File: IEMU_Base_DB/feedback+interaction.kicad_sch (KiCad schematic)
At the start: 37 parts, among them J401 SJ3-35083C-TR, Q401 CSD13381F4, SW401 TS-1088-AR02016, U401 SN74LVC1T45DCKR, U402 DRV5032FADBZR

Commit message: swapped the coin cell vibration actuator pins
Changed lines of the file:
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@@
 	(text "Connector, Lid-Sensor, LEDs & Buttons"
 		(exclude_from_sim no)
-		(at 58.928 25.146 0)
+		(at 78.74 24.892 0)
 		(effects
 			(font

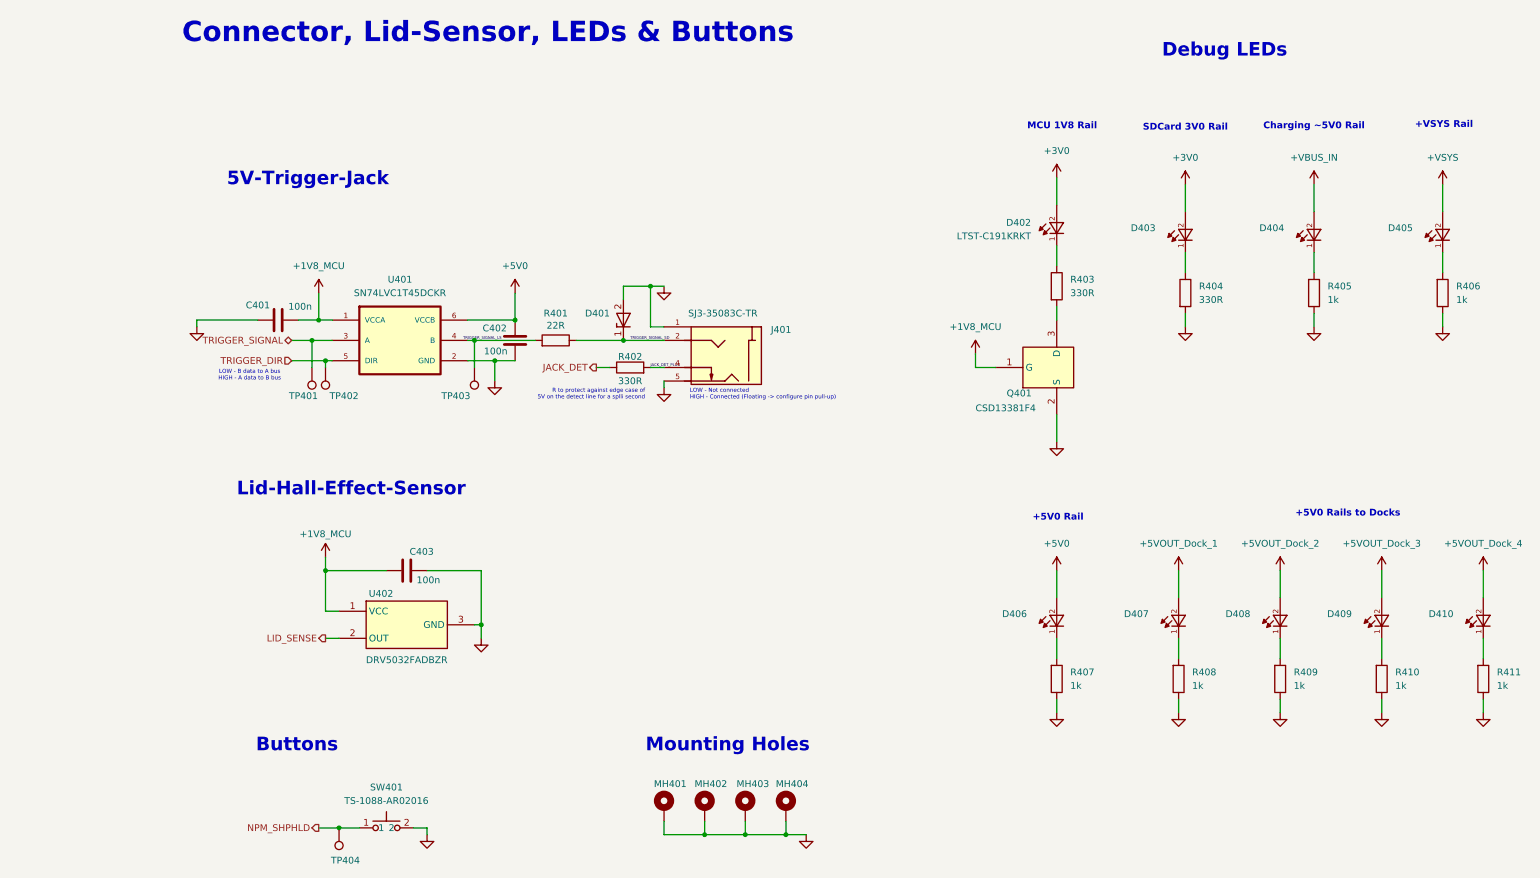
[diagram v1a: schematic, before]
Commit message: implemented changes from the review with TF and fixed lost parts in the library
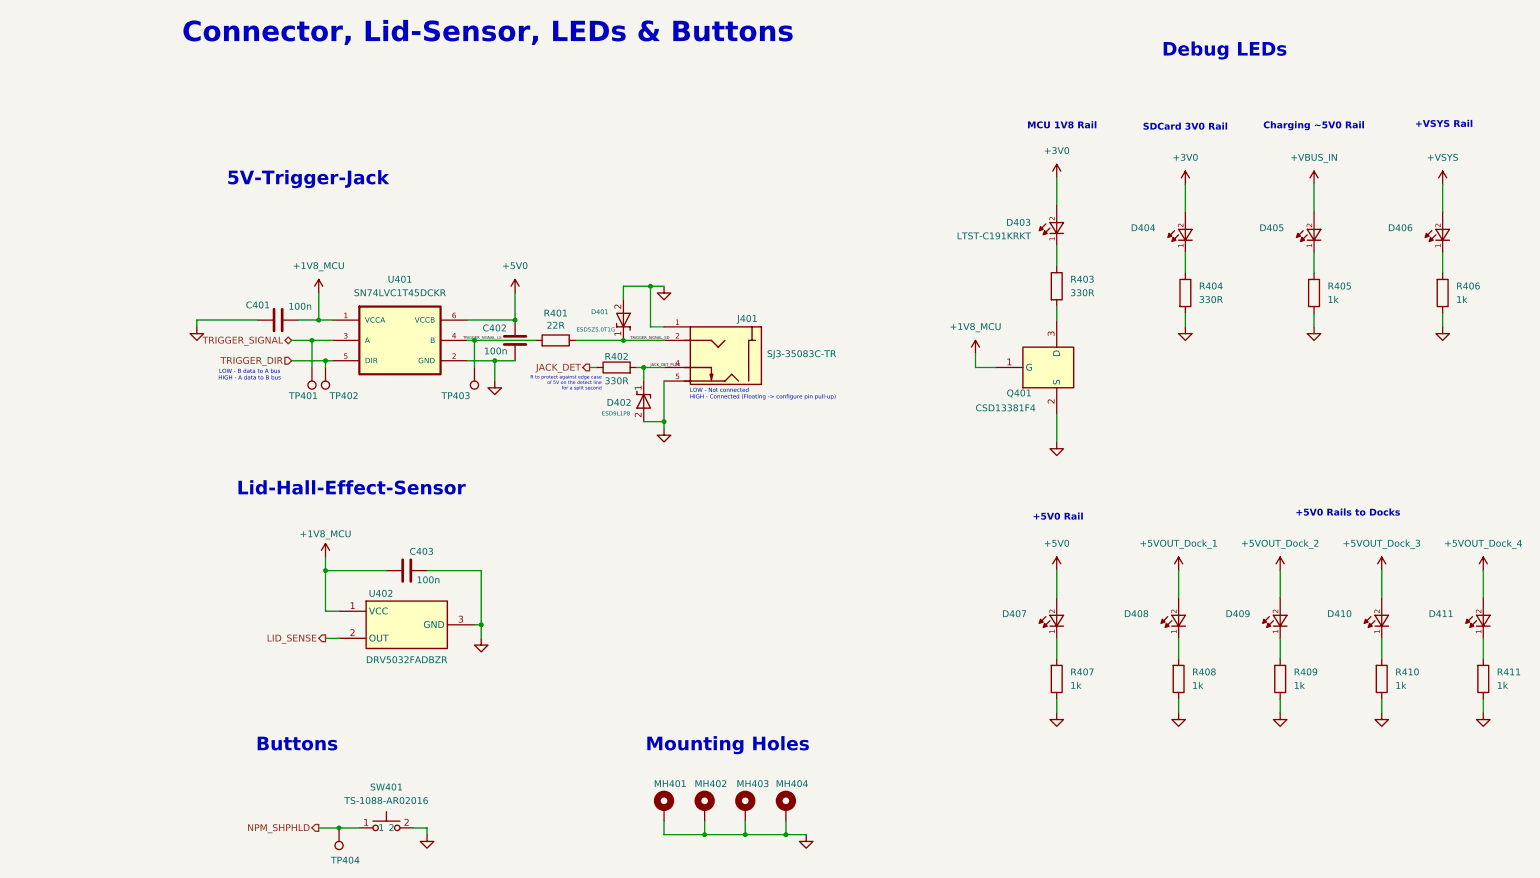
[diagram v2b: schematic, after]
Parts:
- removed D401: TPD1E10B06DYAR, Diode_SMD:D_SOD-523, symbol 0_Power:TPD1E10B06DYAR
- added D401: ESD5Z5.0T1G, Diode_SMD:D_SOD-523_1, symbol 0_Power:ESD5Z5.0T1G
- added D402: ESD9L1P8, Diode_SMD:D_SOD-882, symbol 0_Power:ESD9L1P8
- J401: Distributor Link 2 https://www.digikey.com/en/products/detail/same-sky-formerl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 -> https://www.digikey.de/de/products/detail/same-sky-formerly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
- renumbered D402 to D403, D403 to D404, D404 to D405, D405 to D406, D406 to D407, D407 to D408, D408 to D409, D409 to D410, D410 to D411
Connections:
- net GND: now also D401.2 (GND), D402.2 (GND)
- net JACK_DET_PLUG: now also D402.1 (I/O)
- net TRIGGER_SIGNAL_SD: now also D401.1 (I/O)
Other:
- note added: "R to protect against edge case of 5V on the detect line for a split second"
- note removed: "R to protect against edge case of 5V on the detect line for a splli second"
- moved on the sheet: R402

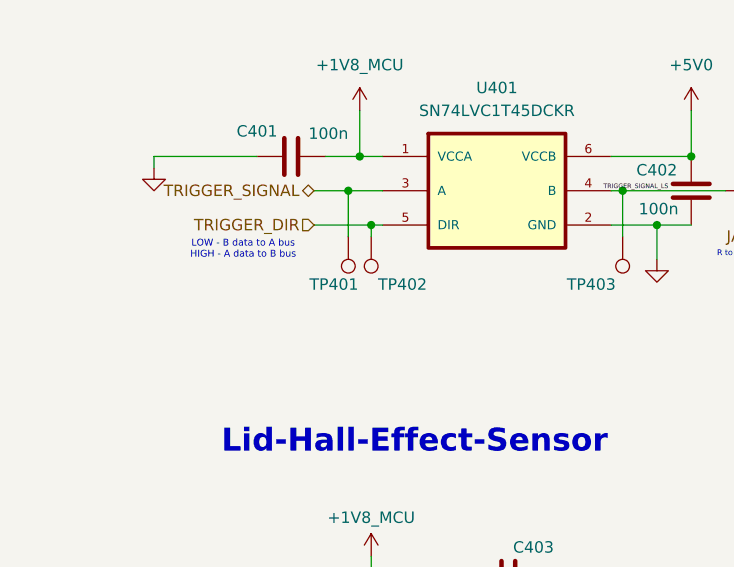
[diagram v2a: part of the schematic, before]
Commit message: layout of base and some fixes on the sensor layout
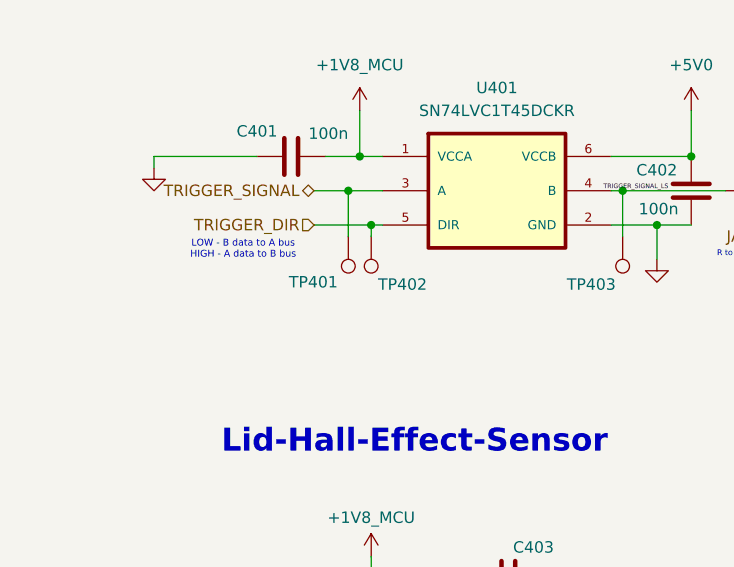
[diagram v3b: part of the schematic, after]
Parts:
- TP401, TP402, TP403, TP404: footprint TestPoint:TestPoint_Pad_D2.0mm -> TestPoint:TestPoint_Pad_D1.0mm
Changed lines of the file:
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@@
 			)
 		)
-		(property "Footprint" "TestPoint:TestPoint_Pad_D2.0mm"
+		(property "Footprint" "TestPoint:TestPoint_Pad_D1.0mm"
 			(at 71.12 87.63 0)
 			(effects
@@
 			)
 		)
-		(property "Footprint" "TestPoint:TestPoint_Pad_D2.0mm"
+		(property "Footprint" "TestPoint:TestPoint_Pad_D1.0mm"
 			(at 53.34 87.63 0)
 			(effects
@@
 			)
 		)
-		(property "Footprint" "TestPoint:TestPoint_Pad_D2.0mm"
+		(property "Footprint" "TestPoint:TestPoint_Pad_D1.0mm"
 			(at 55.88 173.99 0)
 			(effects
@@
 		(dnp no)
 		(property "Reference" "TP401"
-			(at 41.402 92.964 0)
+			(at 39.116 92.71 0)
 			(effects
 				(font
@@
 			)
 		)
-		(property "Footprint" "TestPoint:TestPoint_Pad_D2.0mm"
+		(property "Footprint" "TestPoint:TestPoint_Pad_D1.0mm"
 			(at 50.8 87.63 0)
 			(effects
